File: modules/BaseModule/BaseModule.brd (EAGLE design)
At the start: 100 x 80 mm, 10 parts, among them J1 4P-2.0-90D

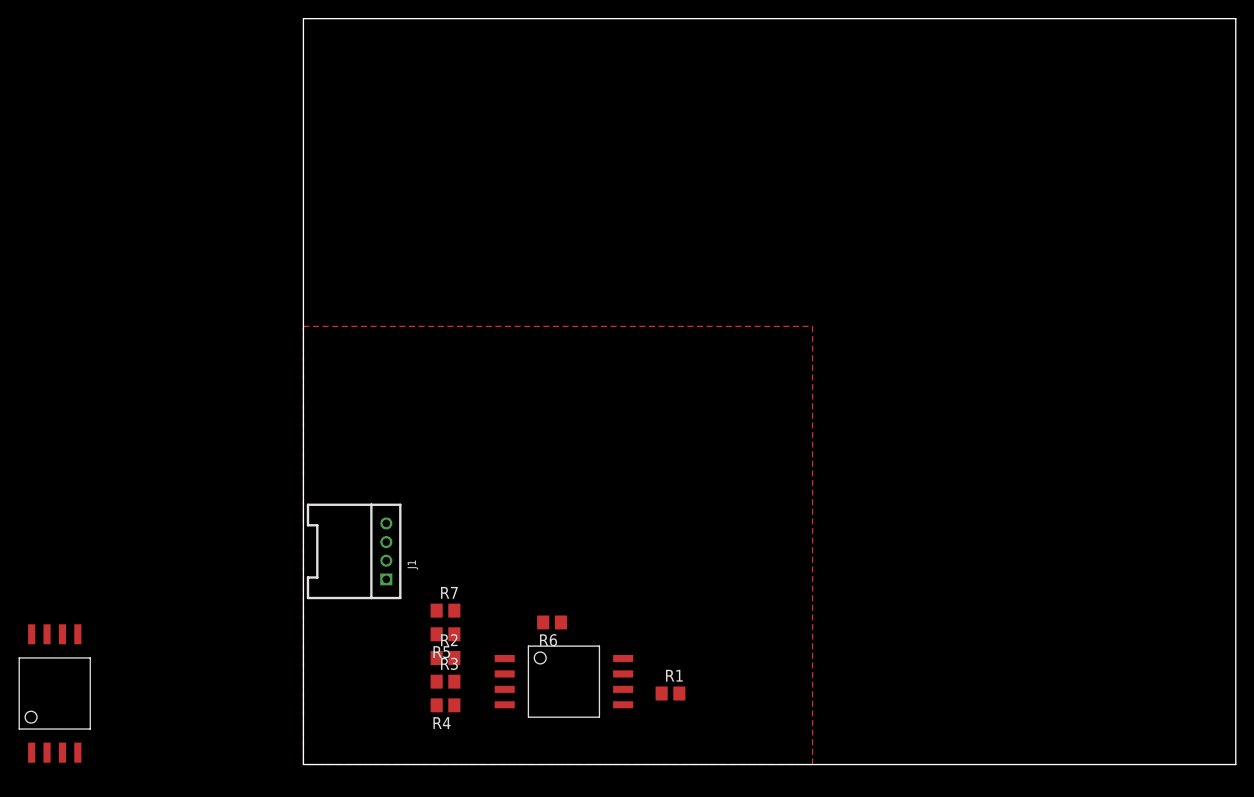
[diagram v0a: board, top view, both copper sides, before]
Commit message: BaseBoard updates + hardware documentation
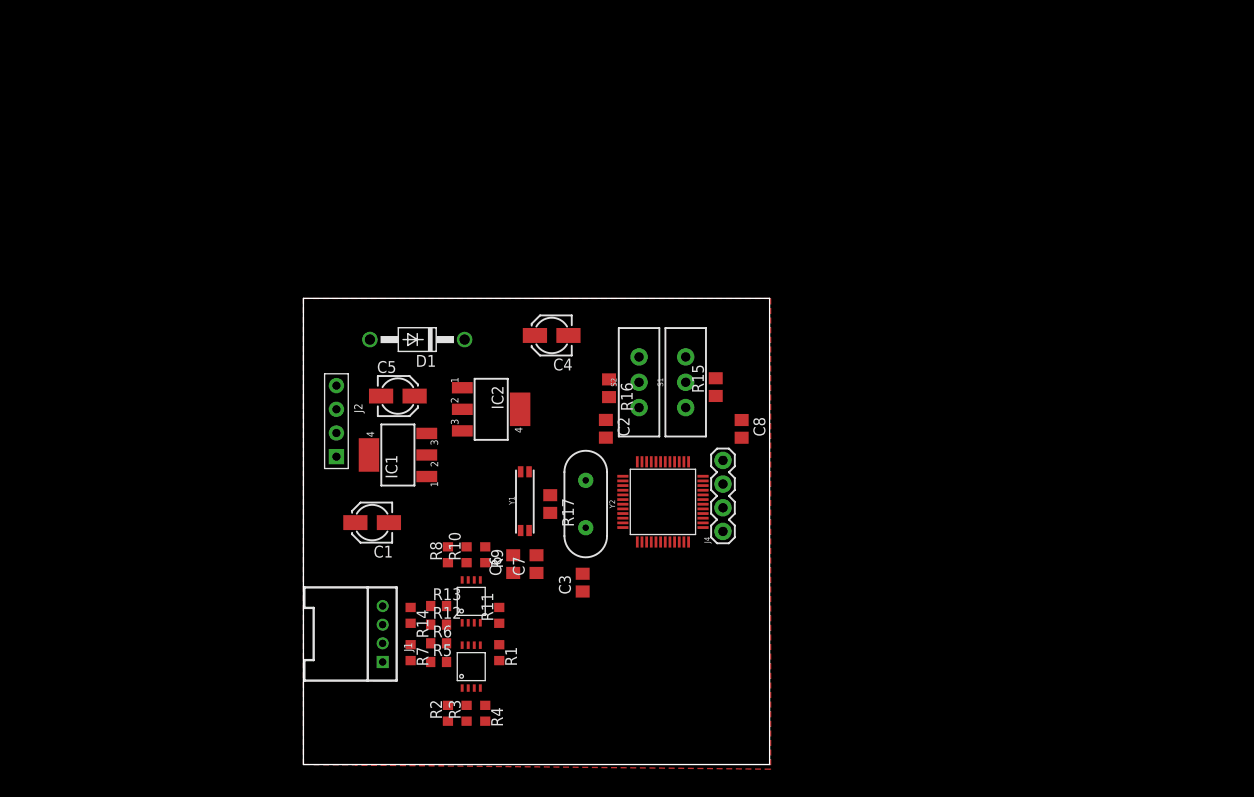
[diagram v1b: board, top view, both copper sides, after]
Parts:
- added C1, C4: 20uF, rcl:153CLV-0405
- added C2, C3, C6, C7, C8: 20pF, rcl:C0805
- added C5: 100uF, rcl:153CLV-0405
- added D1: 1N4004, diode:DO41-10
- added IC1: AMS1117-5.0, linear:SOT223
- added IC2: AMS1117-3.3, linear:SOT223
- added J2: 4p-2.54, Seeed-Connector:H4-2.54
- added J4: (no value), SparkFun-Connectors:1X04
- added R10, R11, R8, R9: 10K, rcl:R0603
- added R12, R13: 20K, rcl:R0603
- added R14: 120R, rcl:R0603
- added R15, R16: 100K, rcl:R0805
- added R17: 1M, rcl:R0805
- added S1, S2: (no value), SparkFun-Switches:SWITCH_SPDT_PTH_11.6X4.0MM_LOCK
- added U$3: STM32F103, Vaello:LQFP48
- added Y1: 32.768kHz, SparkFun-Clocks:CRYSTAL-SMD-MC-146
- added Y2: 8KHz, SparkFun-Clocks:HC49US
- R1, R2, R3, R4, R5, R6, R7: device rcl:R0805 -> rcl:R0603
- moved U$2 45.7 mm to (18.0, 17.5)
- moved R1 18.9 mm to (21.0, 12.0), turned to 270 degrees
- moved R6 12.4 mm to (14.5, 13.0), turned to 0 degrees
- moved U$1 10.1 mm to (18.0, 10.5), turned to 0 degrees
- moved J1 8.87 mm to (8.50, 14.0)
- moved R2 5.94 mm to (15.5, 5.50), turned to 90 degrees
- moved R7 5.86 mm to (11.5, 12.0), turned to 270 degrees
- moved R4 4.34 mm to (19.5, 5.50), turned to 270 degrees
- moved R3 4.07 mm to (17.5, 5.50), turned to 90 degrees
- moved R5 3.06 mm to (14.5, 11.0), turned to 0 degrees
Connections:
- new net +12V: D1.A, J2.3, J2.4
- new net +3V3: C4.+, C8.2, IC2.4, J4.4, S1.1, S2.3, U$3.P$24, U$3.P$36, U$3.P$48, U$3.P$9
- new net BOOT0: R15.1, U$3.P$44
- new net BOOT1: R16.2, U$3.P$20
- new net N$2: R11.1, U$2.3
- new net N$3: R8.1, U$2.6
- new net N$5: R15.2, S1.2
- new net N$6: R16.1, S2.2
- new net N$8: U$3.P$7
- new net N$9: C5.+, D1.C, IC1.3, IC2.3
- new net OSCIN: C2.2, R17.1, U$3.P$5, Y2.1
- new net OSCOUT: C3.2, R17.2, U$3.P$6, Y2.2
- new net PC14: C6.2, U$3.P$3, Y1.P$2
- new net PC15: C7.2, U$3.P$4, Y1.P$1
- new net SWDCLK: J4.2, U$3.P$37
- new net SWDIO: J4.3, U$3.P$34
- net +5V: now also C1.+, IC1.4, R10.1, R10.2, R9.1, R9.2, U$2.2, U$2.4, U$2.5
- net A_IN: now also J1.2; no longer J1.1
- net A_OUT: now also J1.1, R5.1, R7.2, U$1.1; no longer J1.3
- net B_IN: now also J1.4, R13.2, R14.1, U$2.8; no longer J1.2, R5.1, R7.2, U$1.1
- net B_OUT: now also J1.3, R12.1, R14.2, U$2.1; no longer J1.4
- net GND: now also C1.-, C2.1, C3.1, C4.-, C5.-, C6.1, C7.1, C8.1, IC1.1, IC2.1, J2.1, J4.1, R12.2, R13.1, S1.3, S2.1, U$2.7, U$3.P$23, U$3.P$35, U$3.P$47, U$3.P$8
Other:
- board size 100 x 80 mm -> 50 x 50 mm

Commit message: base module update
base module update
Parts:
- added J10, J11, J12, J13, J14, J15, J16, J17, J18, J5, J6, J7, J8, J9: (no value), SparkFun-Connectors:1X08
- added J19, J20: (no value), SparkFun-Connectors:1X02
- added J3: (no value), SparkFun-Connectors:1X14
- moved R9 14.9 mm to (5.00, 25.8), flipped to the bottom, turned to 0 degrees
- moved R1 14.3 mm to (7.75, 6.50), flipped to the bottom
- moved U$1 14.1 mm to (5.00, 5.00)
- moved R11 14.0 mm to (7.75, 20.5), flipped to the bottom
- moved U$2 13.9 mm to (5.00, 22.5)
- moved R3 13.7 mm to (4.50, 1.25), flipped to the bottom, turned to 0 degrees
- moved R15 13.4 mm to (32.2, 46.5)
- moved R10 12.6 mm to (5.00, 23.6), flipped to the bottom, turned to 180 degrees
- moved R4 11.9 mm to (7.75, 3.50), flipped to the bottom, turned to 90 degrees
- moved R5 11.4 mm to (4.50, 5.50), flipped to the bottom
- moved R7 11.4 mm to (1.50, 6.50), flipped to the bottom
- moved R6 11.3 mm to (4.50, 7.75), flipped to the bottom
- moved R2 11.2 mm to (4.50, 3.25), flipped to the bottom, turned to 0 degrees
- moved C7 11.2 mm to (20.0, 31.5), turned to 0 degrees
- moved R13 10.5 mm to (5.00, 21.5), flipped to the bottom
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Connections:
- new net RX1: J19.1, R4.2, R8.2, U$3.P$31
- new net RX2: J20.1, R11.2, U$3.P$13
- new net TX1: J19.2, R1.2, U$3.P$30
- new net TX2: J20.2, U$3.P$12
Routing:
- net B_IN: track 0.00 -> 19.7 mm, vias 0 -> 2
- net +5V: track 0.00 -> 19.2 mm, vias 0 -> 1
- net B_OUT: track 0.00 -> 17.8 mm, vias 0 -> 1
- net N$3: track 0.00 -> 6.92 mm, vias 0 -> 1
- net N$2: track 0.00 -> 4.63 mm, vias 0 -> 1
- net RX1: track 0.00 -> 3.10 mm
- added copper zone on layer 16, net GND
